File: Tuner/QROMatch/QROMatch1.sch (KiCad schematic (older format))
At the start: 78 parts, among them J1 Conn_02x12_Odd_Even, J3 Conn_01x06

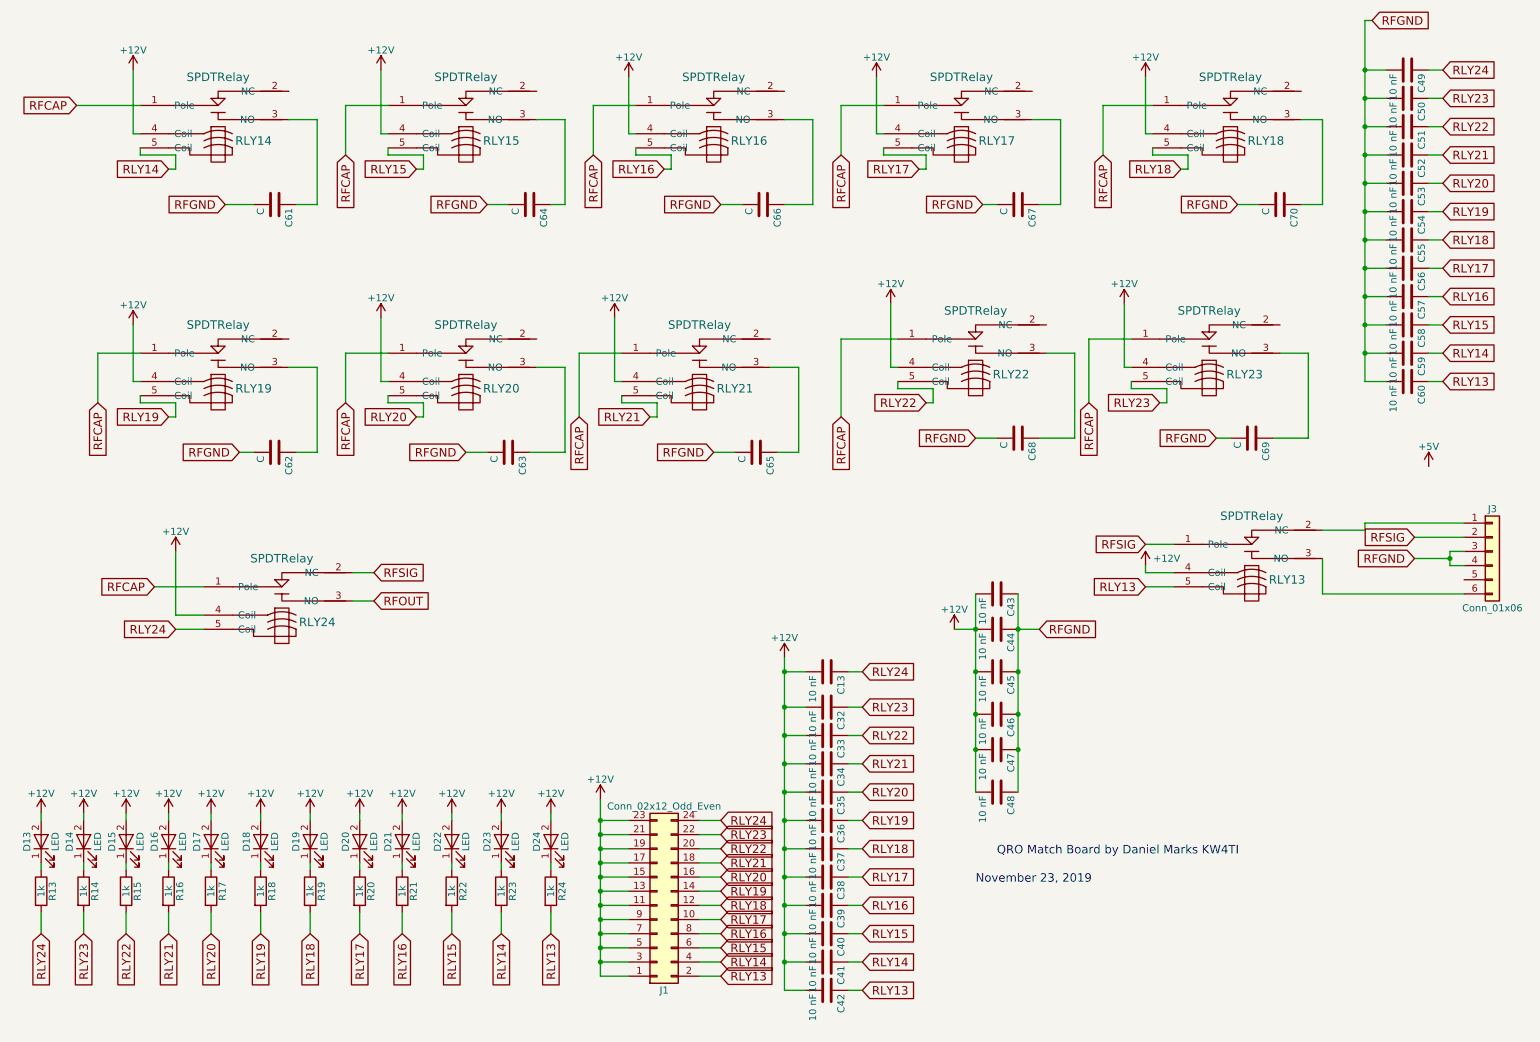
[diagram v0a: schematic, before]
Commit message: Changed capacitance high-Z low-Z to have less series inductance
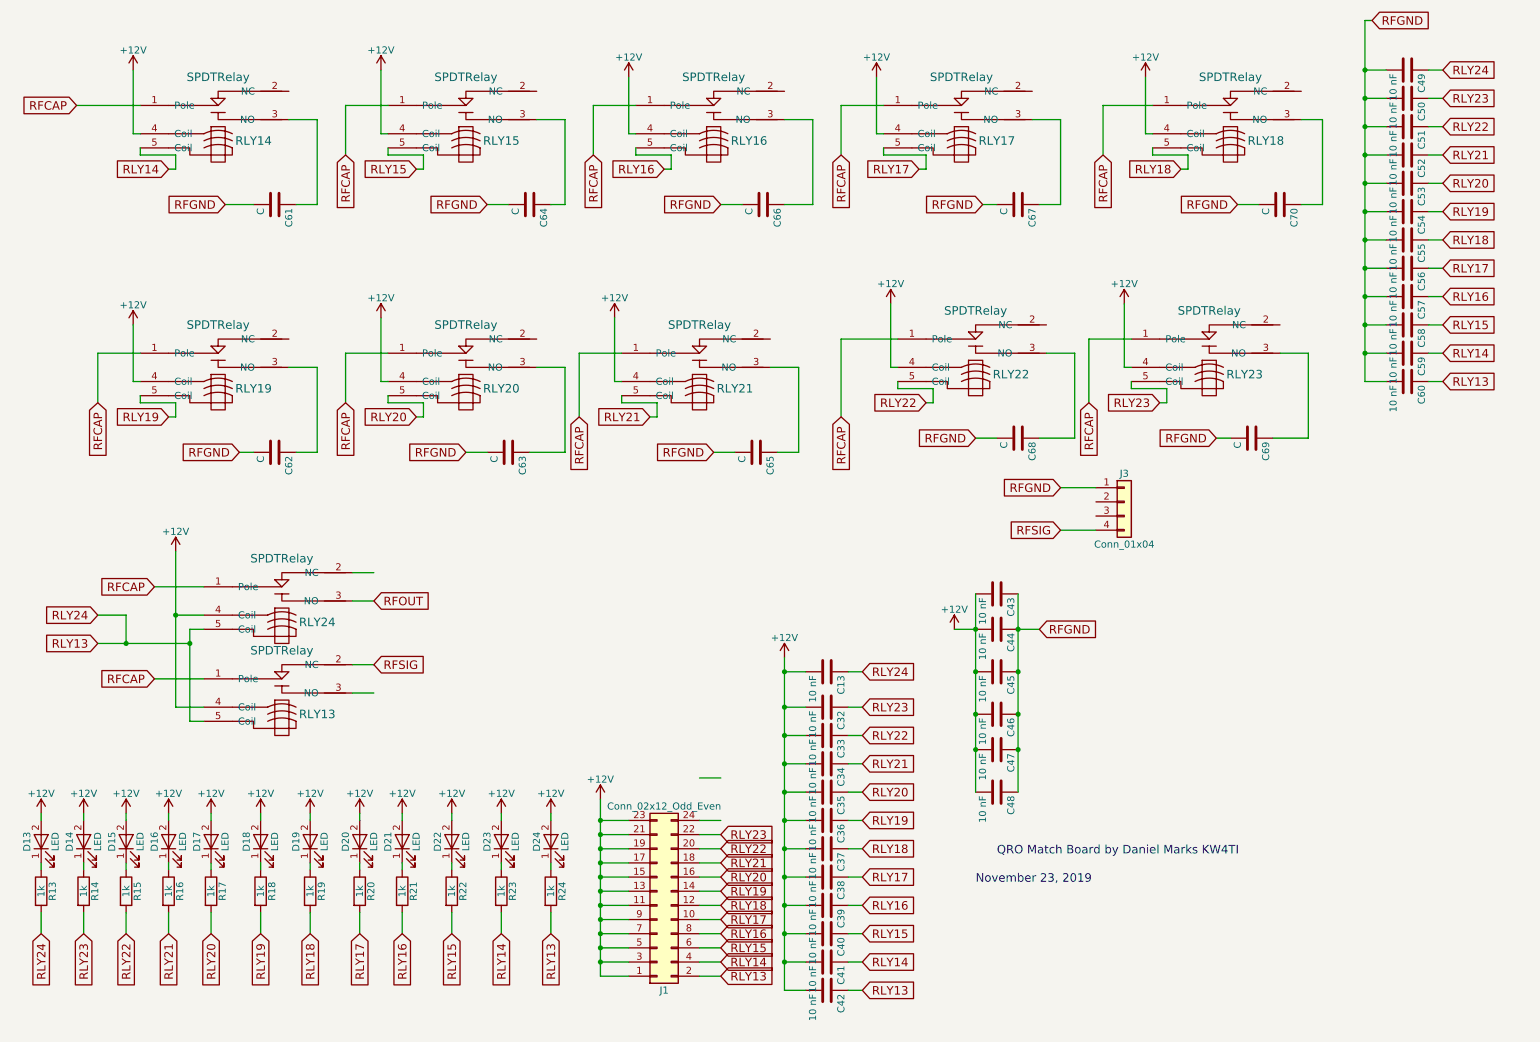
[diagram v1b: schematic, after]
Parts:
- removed J3: Conn_01x06, Connectors_Terminal_Blocks:TerminalBlock_bornier-6_P5.08mm, symbol Conn_01x06
- added J3: Conn_01x04, Connectors_Terminal_Blocks:TerminalBlock_bornier-4_P5.08mm, symbol Conn_01x04
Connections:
- net RFCAP: now also RLY13.1 (Pole)
- net RFGND: now also J3.1 (Pin_1)
- net RFSIG: now also RLY13.2 (NC), J3.4 (Pin_4); no longer RLY13.1 (Pole), RLY24.2 (NC)
- net RLY13: now also C13.1, C49.1, R13.2, RLY24.5 (Coil)
- removed net RLY24: C13.1, C49.1, J1.24 (Pin_24), R13.2, RLY24.5 (Coil)
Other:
- moved on the sheet: RLY13

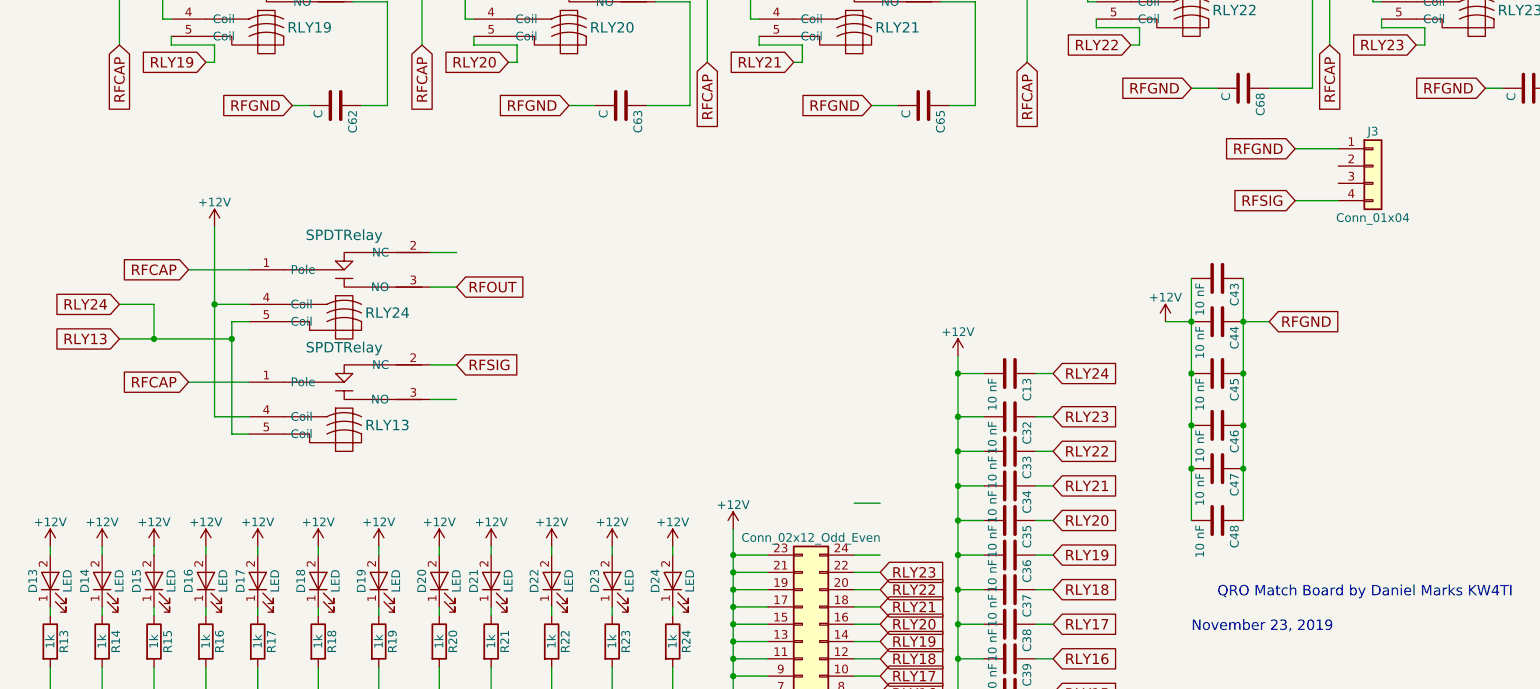
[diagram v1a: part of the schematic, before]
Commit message: Added extra capacitors between relay power and ground posts
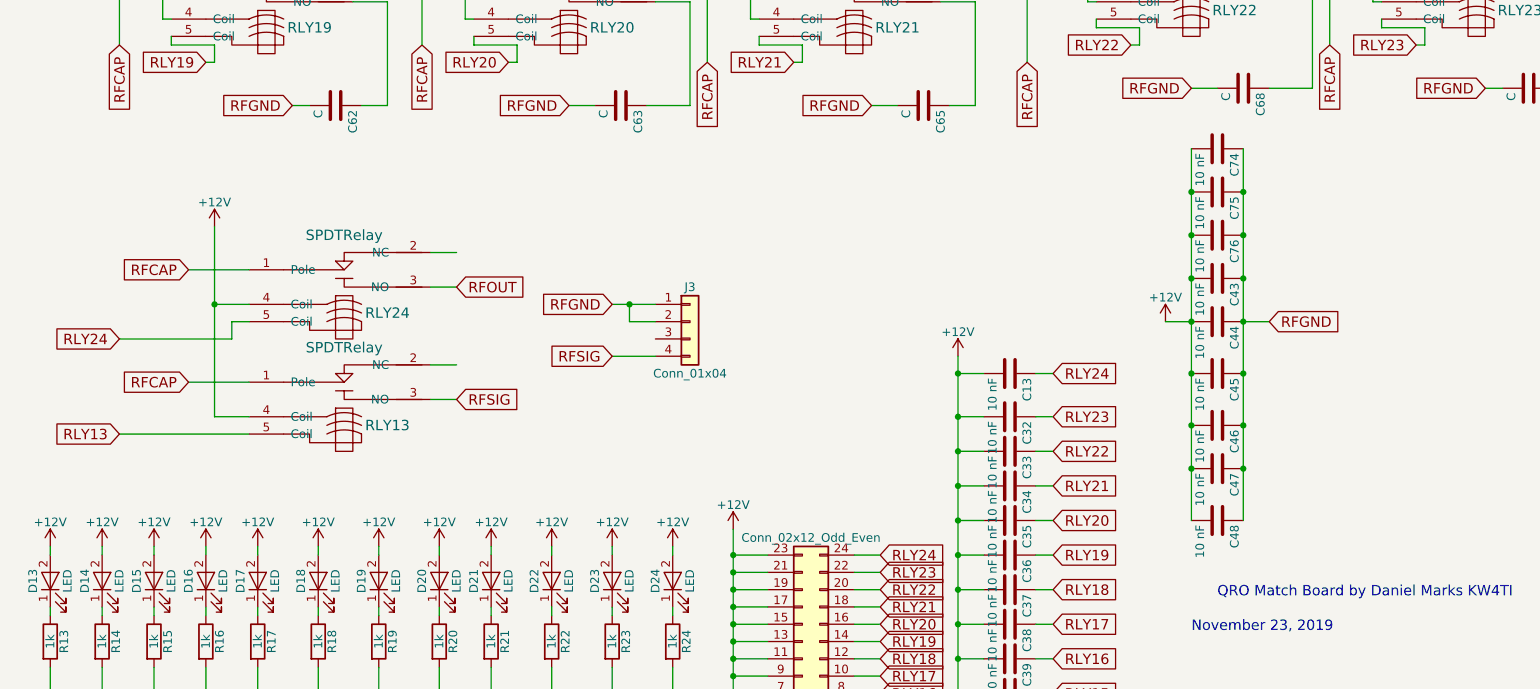
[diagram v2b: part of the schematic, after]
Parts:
- added C74, C75, C76: 10 nF, Capacitors_THT:C_Disc_D5.0mm_W2.5mm_P2.50mm, symbol C
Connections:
- net +12V: now also C74.2, C75.2, C76.2
- net RFGND: now also J3.2 (Pin_2), C74.1, C75.1, C76.1
- net RFSIG: now also RLY13.3 (NO); no longer RLY13.2 (NC)
- net RLY13: no longer C13.1, C49.1, R13.2, RLY24.5 (Coil)
- net RLY24: now reaches J1.24 (Pin_24)
- net RLY24: now also C13.1, C49.1, R13.2, RLY24.5 (Coil)
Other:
- moved on the sheet: J3
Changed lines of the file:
@@
 Text GLabel 3100 4850 2    60   Input ~ 0
 RFOUT
-Text GLabel 3100 5300 2    60   Input ~ 0
+Text GLabel 3100 5500 2    60   Input ~ 0
 RFSIG
 $Comp
@@
 	0    1    1    0
 $EndComp
-Text GLabel 7950 4050 0    60   Input ~ 0
+Text GLabel 4000 4950 0    60   Input ~ 0
 RFGND
 $Comp
@@
 	10100 750  10150 750
 Wire Wire Line
-	7650 4800 7650 6200
+	7650 4050 7650 6200
 Connection ~ 7650 5050
 Connection ~ 7650 5350
@@
 Connection ~ 7650 5900
 Wire Wire Line
-	7350 4800 7350 6200
+	7350 4050 7350 6200
 Connection ~ 7350 5900
 Connection ~ 7350 5650
@@
 Wire Wire Line
 	3100 4650 2950 4650
-Text GLabel 7950 4350 0    60   Input ~ 0
+Text GLabel 4000 5250 0    60   Input ~ 0
 RFSIG
 Text GLabel 1550 4750 0    60   Input ~ 0
@@
 Connection ~ 1700 4950
 Wire Wire Line
-	1800 5050 1800 5700
-Wire Wire Line
-	1800 5700 1900 5700
+	1800 5050 1800 5150
+Wire Wire Line
+	1150 5700 1900 5700
 $Comp
 L Conn_01x04 J3
 U 1 1 5DDA2558
-P 8400 4150
-F 0 "J3" H 8400 4350 50  0000 C CNN
-F 1 "Conn_01x04" H 8400 3850 50  0000 C CNN
-F 2 "Connectors_Terminal_Blocks:TerminalBlock_bornier-4_P5.08mm" H 8400 4150 50  0001 C CNN
-F 3 "" H 8400 4150 50  0001 C CNN
-	1    8400 4150
-	1    0    0    -1
-$EndComp
-Wire Wire Line
-	8200 4350 7950 4350
-Wire Wire Line
-	7950 4050 8200 4050
+P 4450 5050
+F 0 "J3" H 4450 5250 50  0000 C CNN
+F 1 "Conn_01x04" H 4450 4750 50  0000 C CNN
+F 2 "Connectors_Terminal_Blocks:TerminalBlock_bornier-4_P5.08mm" H 4450 5050 50  0001 C CNN
+F 3 "" H 4450 5050 50  0001 C CNN
+	1    4450 5050
+	1    0    0    -1
+$EndComp
+Wire Wire Line
+	4250 5250 4000 5250
+Wire Wire Line
+	4000 4950 4250 4950
 Wire Wire Line
 	3100 5300 2950 5300
-Text GLabel 1150 5150 0    60   Input ~ 0
+Text GLabel 1150 5700 0    60   Input ~ 0
 RLY13
 Wire Wire Line
-	1150 5150 1800 5150
-Connection ~ 1800 5150
+	1800 5150 1150 5150
 Text GLabel 10650 1100 2    60   Input ~ 0
 RLY24
 Text GLabel 750  7200 3    60   Input ~ 0
 RLY24
-Text GLabel 1150 4950 0    60   Input ~ 0
+Text GLabel 1150 5150 0    60   Input ~ 0
 RLY24
 Wire Wire Line
-	5550 6100 5400 6100
-Wire Wire Line
 	1900 4950 1700 4950
-Wire Wire Line
-	1150 4950 1350 4950
-Wire Wire Line
-	1350 4950 1350 5150
-Connection ~ 1350 5150
+Text GLabel 5550 6400 2    60   Input ~ 0
+RLY24
+$Comp
+L C C76
+U 1 1 5DDAC7AB
+P 7500 4550
+F 0 "C76" H 7525 4650 50  0000 L CNN
+F 1 "10 nF" H 7525 4450 50  0000 L CNN
+F 2 "Capacitors_THT:C_Disc_D5.0mm_W2.5mm_P2.50mm" H 7538 4400 50  0001 C CNN
+F 3 "" H 7500 4550 50  0001 C CNN
+	1    7500 4550
+	0    1    1    0
+$EndComp
+$Comp
+L C C75
+U 1 1 5DDACB1B
+P 7500 4300
+F 0 "C75" H 7525 4400 50  0000 L CNN
+F 1 "10 nF" H 7525 4200 50  0000 L CNN
+F 2 "Capacitors_THT:C_Disc_D5.0mm_W2.5mm_P2.50mm" H 7538 4150 50  0001 C CNN
+F 3 "" H 7500 4300 50  0001 C CNN
+	1    7500 4300
+	0    1    1    0
+$EndComp
+$Comp
+L C C74
+U 1 1 5DDACC1F
+P 7500 4050
+F 0 "C74" H 7525 4150 50  0000 L CNN
+F 1 "10 nF" H 7525 3950 50  0000 L CNN
+F 2 "Capacitors_THT:C_Disc_D5.0mm_W2.5mm_P2.50mm" H 7538 3900 50  0001 C CNN
+F 3 "" H 7500 4050 50  0001 C CNN
+	1    7500 4050
+	0    1    1    0
+$EndComp
+Connection ~ 7350 4300
+Connection ~ 7350 4800
+Connection ~ 7350 4550
+Connection ~ 7650 4800
+Connection ~ 7650 4550
+Connection ~ 7650 4300
+Wire Wire Line
+	4100 4950 4100 5050
+Wire Wire Line
+	4100 5050 4250 5050
+Connection ~ 4100 4950
 $EndSCHEMATC

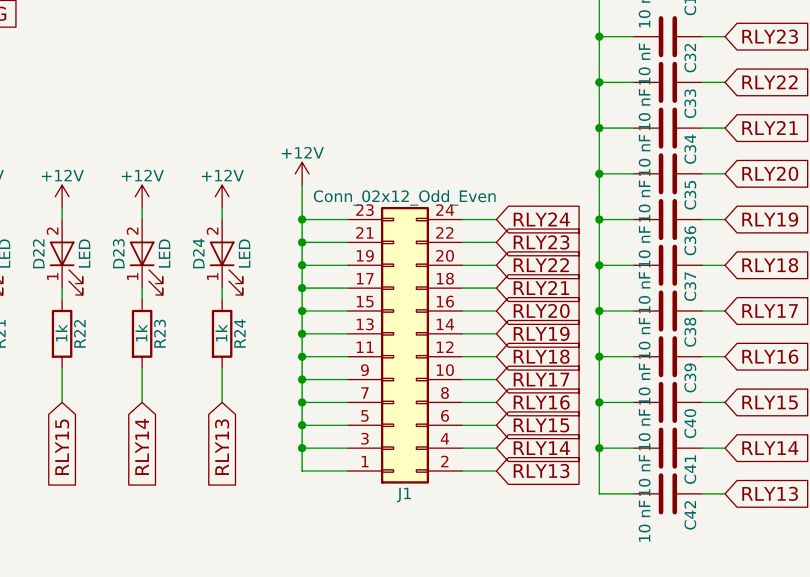
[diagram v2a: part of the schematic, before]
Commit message: Changed from 2x12 IDC to more common 2x13 IDC
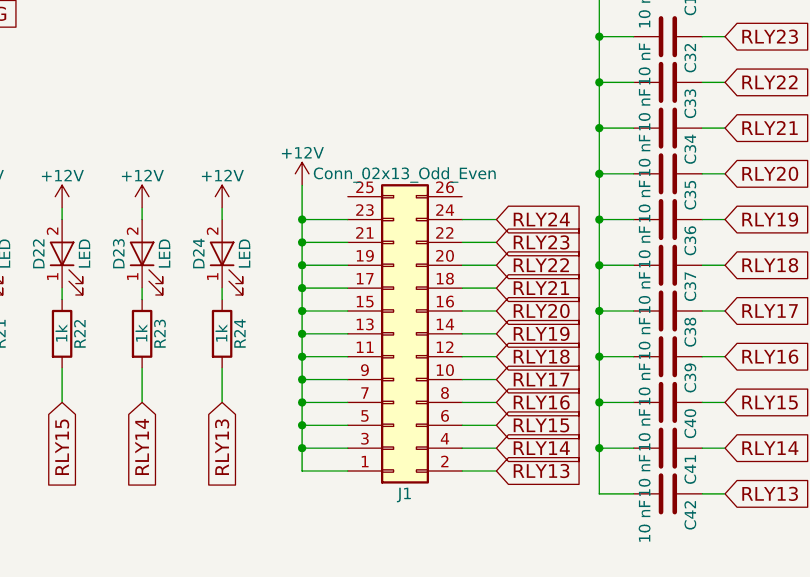
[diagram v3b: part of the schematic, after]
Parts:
- removed J1: Conn_02x12_Odd_Even, Pin_Headers:Pin_Header_Straight_2x12_Pitch2.54mm, symbol Conn_02x12_Odd_Even
- added J1: Conn_02x13_Odd_Even, Pin_Headers:Pin_Header_Straight_2x13_Pitch2.54mm, symbol Conn_02x13_Odd_Even
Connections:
- net +12V: now also J1.1 (Pin_1), J1.11 (Pin_11), J1.13 (Pin_13), J1.15 (Pin_15), J1.17 (Pin_17), J1.19 (Pin_19), J1.21 (Pin_21), J1.23 (Pin_23), J1.3 (Pin_3), J1.5 (Pin_5), J1.7 (Pin_7), J1.9 (Pin_9)
- net RLY13: now also J1.2 (Pin_2)
- net RLY14: now also J1.4 (Pin_4)
- net RLY15: now also J1.6 (Pin_6)
- net RLY16: now also J1.8 (Pin_8)
- net RLY17: now also J1.10 (Pin_10)
- net RLY18: now also J1.12 (Pin_12)
- net RLY19: now also J1.14 (Pin_14)
- net RLY20: now also J1.16 (Pin_16)
- net RLY21: now also J1.18 (Pin_18)
- net RLY22: now also J1.20 (Pin_20)
- net RLY23: now also J1.22 (Pin_22)
- net RLY24: now also J1.24 (Pin_24)
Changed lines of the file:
@@
 Text GLabel 3100 5500 2    60   Input ~ 0
 RFSIG
-$Comp
-L Conn_02x12_Odd_Even J1
-U 1 1 5DDA7736
-P 5100 7000
-F 0 "J1" H 5150 7600 50  0000 C CNN
-F 1 "Conn_02x12_Odd_Even" H 5150 6300 50  0000 C CNN
-F 2 "Pin_Headers:Pin_Header_Straight_2x12_Pitch2.54mm" H 5100 7000 50  0001 C CNN
-F 3 "" H 5100 7000 50  0001 C CNN
-	1    5100 7000
-	1    0    0    1
-$EndComp
 Text GLabel 5550 6500 2    60   Input ~ 0
 RLY23
@@
 	4100 5050 4250 5050
 Connection ~ 4100 4950
+$Comp
+L Conn_02x13_Odd_Even J1
+U 1 1 5DE1EB52
+P 5100 6900
+F 0 "J1" H 5150 7600 50  0000 C CNN
+F 1 "Conn_02x13_Odd_Even" H 5150 6200 50  0000 C CNN
+F 2 "Pin_Headers:Pin_Header_Straight_2x13_Pitch2.54mm" H 5100 6900 50  0001 C CNN
+F 3 "" H 5100 6900 50  0001 C CNN
+	1    5100 6900
+	1    0    0    1
+$EndComp
 $EndSCHEMATC
